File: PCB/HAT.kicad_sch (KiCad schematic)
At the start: 0 parts

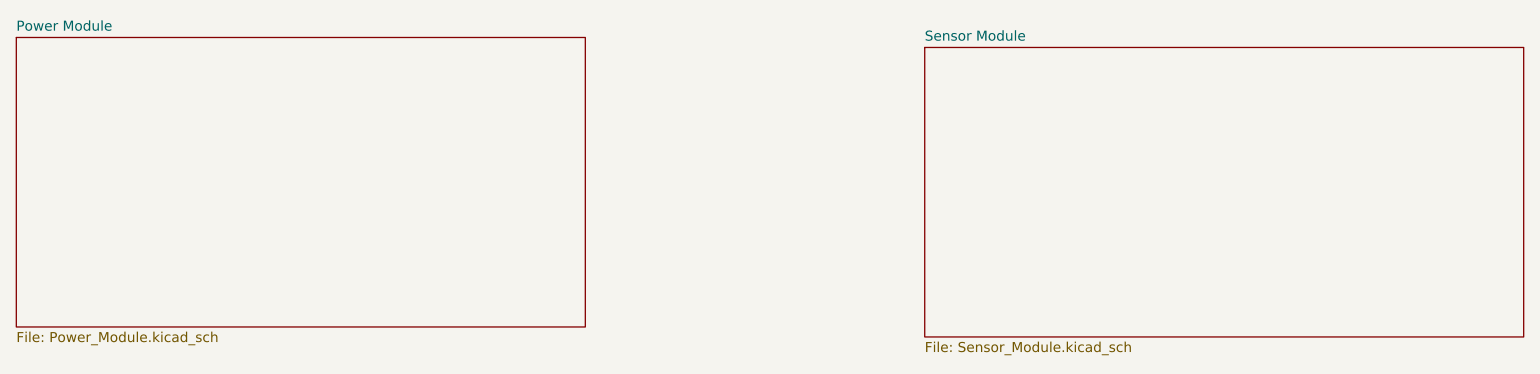
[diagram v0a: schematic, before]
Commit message: progress w/ power module schematic, updated BOM
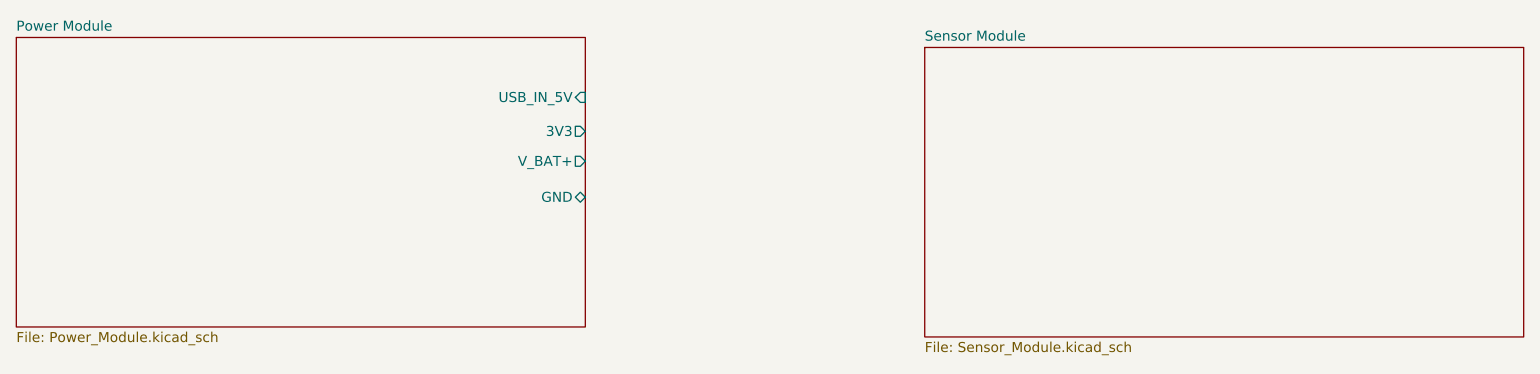
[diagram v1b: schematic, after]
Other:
- sheet Power Module ports: added 3V3, GND, USB_IN_5V, V_BAT+; removed none
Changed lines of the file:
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@@
       (effects (font (size 1.27 1.27)) (justify left top))
+    )
+    (pin "USB_IN_5V" input (at 113.03 38.1 0)
+      (effects (font (size 1.27 1.27)) (justify right))
+    )
+    (pin "3V3" output (at 113.03 42.418 0)
+      (effects (font (size 1.27 1.27)) (justify right))
+    )
+    (pin "V_BAT+" output (at 113.03 46.228 0)
+      (effects (font (size 1.27 1.27)) (justify right))
+    )
+    (pin "GND" bidirectional (at 113.03 50.8 0)
+      (effects (font (size 1.27 1.27)) (justify right))
     )
     (instances

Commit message: made a bunch of progress with design of UVLO and PP
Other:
- company: (none) -> Group 3
- title: (none) -> Environment Sensing HAT For STM32
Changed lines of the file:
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@@
 (kicad_sch (version 20230121) (generator eeschema)
   (paper "A4")
+  (title_block
+    (title "Environment Sensing HAT For STM32")
+    (date "2023-03-10")
+    (rev "v0.0.1")
+    (company "Group 3")
+  )
   (sheet (at 40.64 30.48) (size 72.39 36.83) (fields_autoplaced)
     (stroke (width 0.1524) (type solid))
